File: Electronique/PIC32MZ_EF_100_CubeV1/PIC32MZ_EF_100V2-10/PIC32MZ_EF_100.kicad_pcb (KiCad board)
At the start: 2 copper layers, 95.2 x 95.2 mm, 86 parts, among them J1001 Conn_02x20_Odd_Even, J1002 Conn_02x20_Odd_Even, J1003 Conn_01x04, J1004 USB_B_Mini, J1005 RJ12, J2001 Conn_02x05_Top_Bottom, J2002 Conn_02x05_Top_Bottom, Q2001 BC817, Q2002 BC817, Q3001 2N7002, Q3002 2N7002, Q3003 2N7002, SW1001 SW_Push, U2001 PCF8563T, U2002 MCP1501-SN, U3001 24LC1025, U3002 LM75A, U3003 SAA1064T, U3004 PIC32MZ2048EF100, X3001 32.768KHz, Y2001 24Mhz, Y2003 Crystal

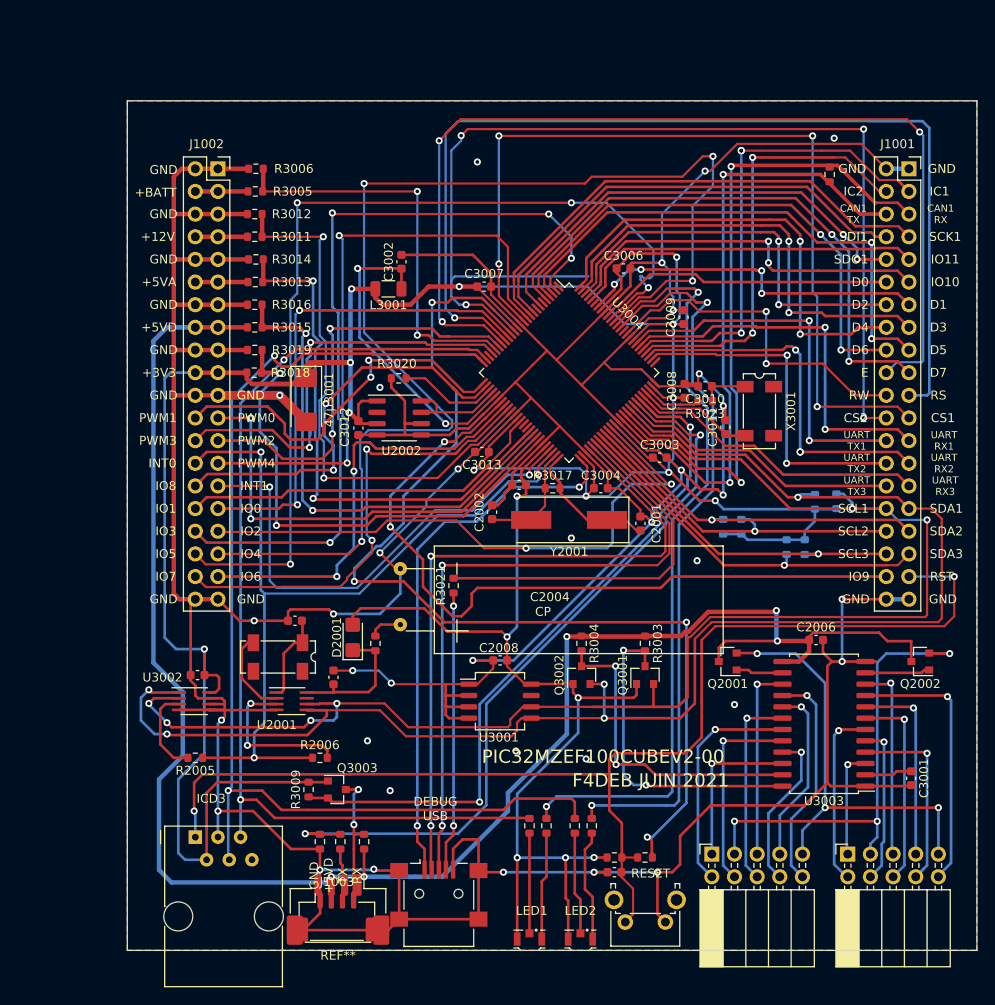
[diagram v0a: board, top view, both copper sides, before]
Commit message: V206 TM1638 7Segments Begin
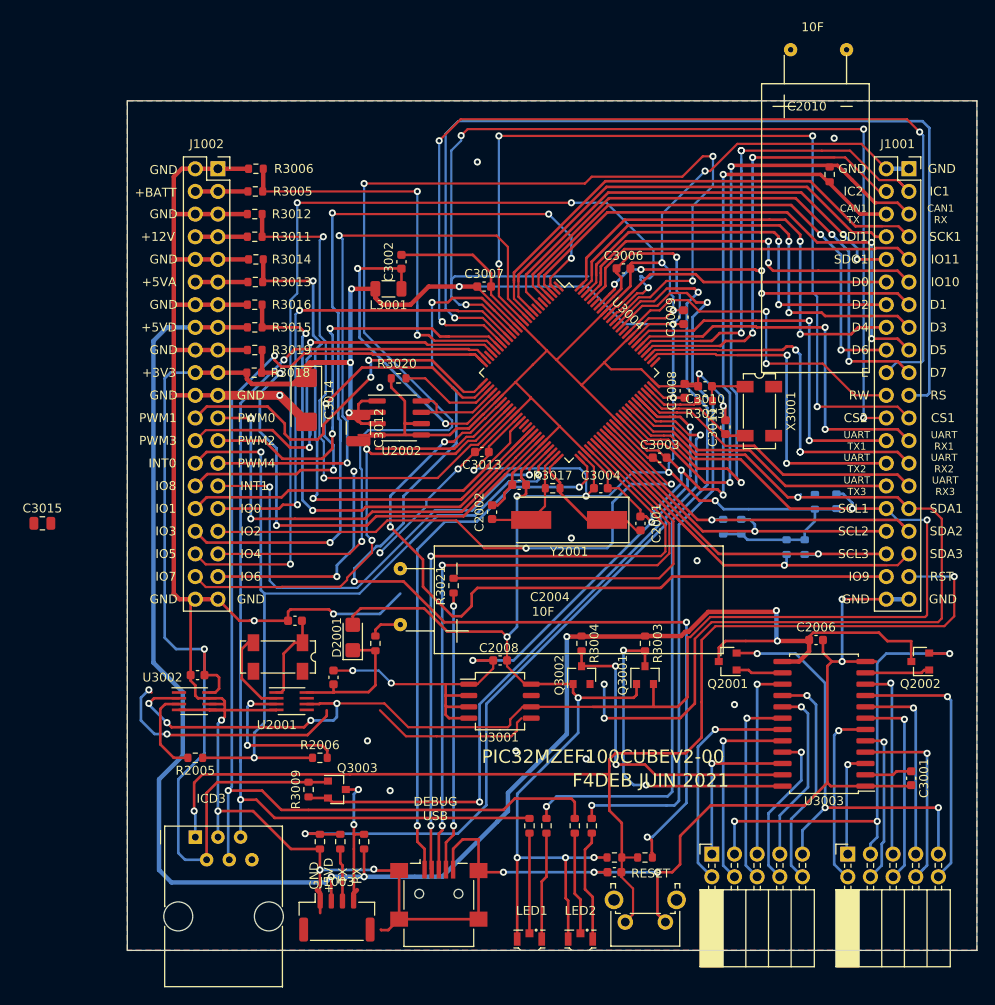
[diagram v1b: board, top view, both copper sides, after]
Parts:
- removed REF**: JST_ZE_BM04B-ZESS-TBT_1x04-1MP_P1.50mm_Vertical, Connector_JST:JST_ZE_BM04B-ZESS-TBT_1x04-1MP_P1.50mm_Vertical
- added C2010: 10F, CEN-PCB:C-10F, F.Cu at (180.3, 45.1)
- added C3015: 220p, Capacitor_SMD:C_0805_2012Metric, F.Cu at (99.7, 94.4)
- C2004: value CP -> 10F
- C3012: value 100n -> 2.2µF; footprint Capacitor_SMD:C_0603_1608Metric -> Capacitor_SMD:C_1210_3225Metric
- C3014: renamed from 47µ3001; value CP -> 47µ
- L3001: value L -> 15µH
- Q2001, Q2002: value BC817 -> BSR19
- R3005, R3011, R3013, R3015, R3018: value R -> 10k
- R3006, R3012: value R -> 1k5
- R3014, R3016, R3019: value R -> 4k7
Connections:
- C2004 pad 2: GND -> Net-(C2004-Pad2)
- J1003 pad MP: GND -> (no net)
- Q3002 pad 2: /SDA1 -> /I2C/SDA1
- R3001 pad 2: /SDA1 -> /I2C/SDA1
- U2001 pad 5: /SDA1 -> /I2C/SDA1
- U3001 pad 5: /SDA1 -> /I2C/SDA1
- U3002 pad 1: /SDA1 -> /I2C/SDA1
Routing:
- net /SDA1: track 173.6 -> 147.6 mm
- net GND: track 688.4 -> 669.3 mm
- net /IO6: track 48.3 -> 42.5 mm
